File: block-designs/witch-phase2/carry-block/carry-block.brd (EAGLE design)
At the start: 27.9 x 27.9 mm, 13 parts, among them IC1 74AHC1G32DBV, IC2 74AHC1G86DBV, IC3 74LS195D, IC4 741G175

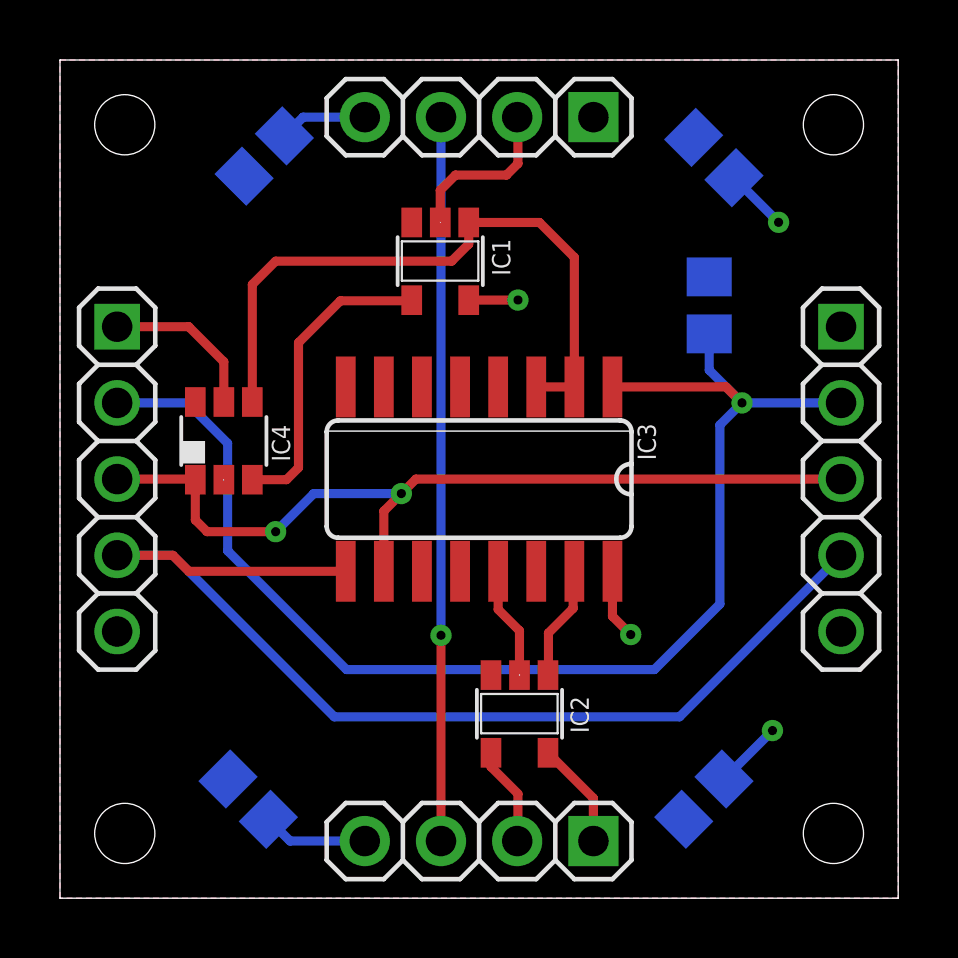
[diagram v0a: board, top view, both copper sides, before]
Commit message: adjust borders for ground/vcc plains and size to match 1.1inch grids
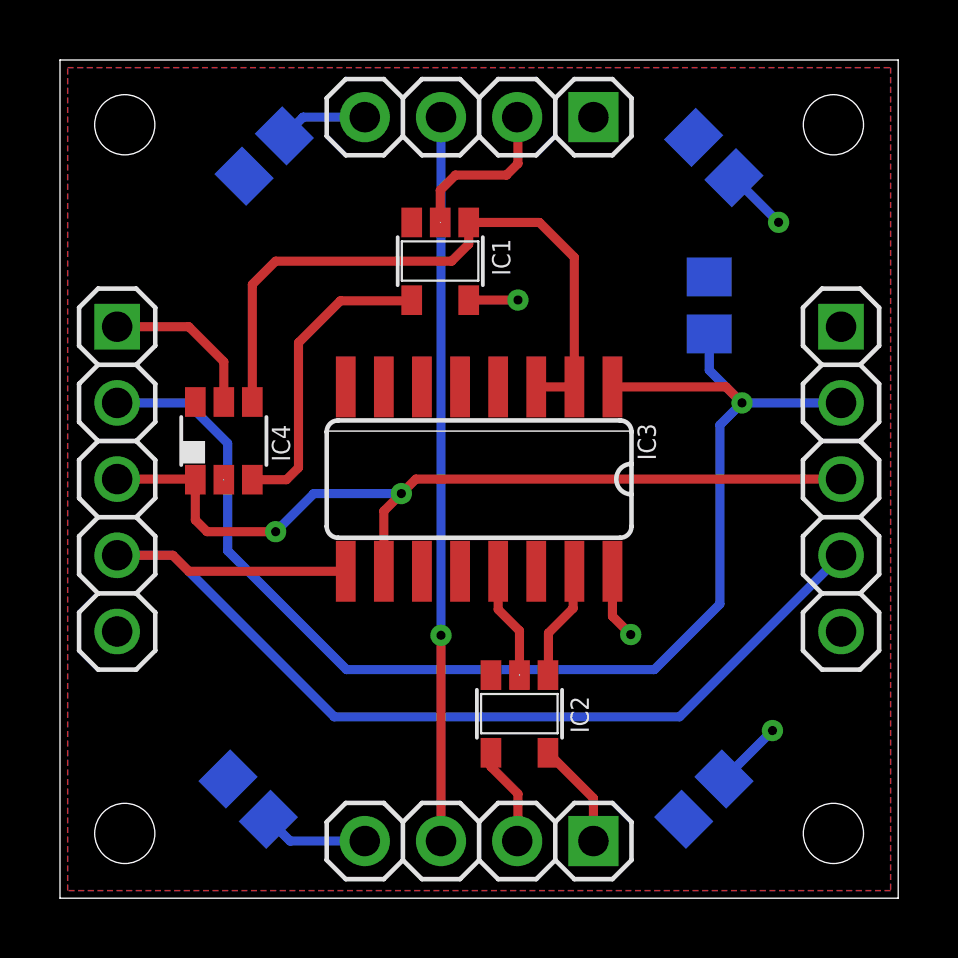
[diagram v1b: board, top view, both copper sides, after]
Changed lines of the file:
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@@
 <contactref element="JP1" pad="4"/>
 <contactref element="JP3" pad="4"/>
-<polygon width="0" layer="1">
-<vertex x="27.94" y="0"/>
-<vertex x="0" y="0"/>
-<vertex x="0" y="27.94"/>
-<vertex x="27.94" y="27.94"/>
+<polygon width="0.254" layer="1">
+<vertex x="27.686" y="0.254"/>
+<vertex x="0.254" y="0.254"/>
+<vertex x="0.254" y="27.686"/>
+<vertex x="27.686" y="27.686"/>
 </polygon>
 <contactref element="IC1" pad="3"/>
@@
 <contactref element="JP1" pad="1"/>
 <contactref element="JP3" pad="1"/>
-<polygon width="0" layer="16">
-<vertex x="27.94" y="0"/>
-<vertex x="0" y="0"/>
-<vertex x="0" y="27.94"/>
-<vertex x="27.94" y="27.94"/>
+<polygon width="0.254" layer="16">
+<vertex x="27.686" y="0.254"/>
+<vertex x="0.254" y="0.254"/>
+<vertex x="0.254" y="27.686"/>
+<vertex x="27.686" y="27.686"/>
 </polygon>
 <contactref element="JP4" pad="1"/>

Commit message: updated board layout pictures and pdf schematics
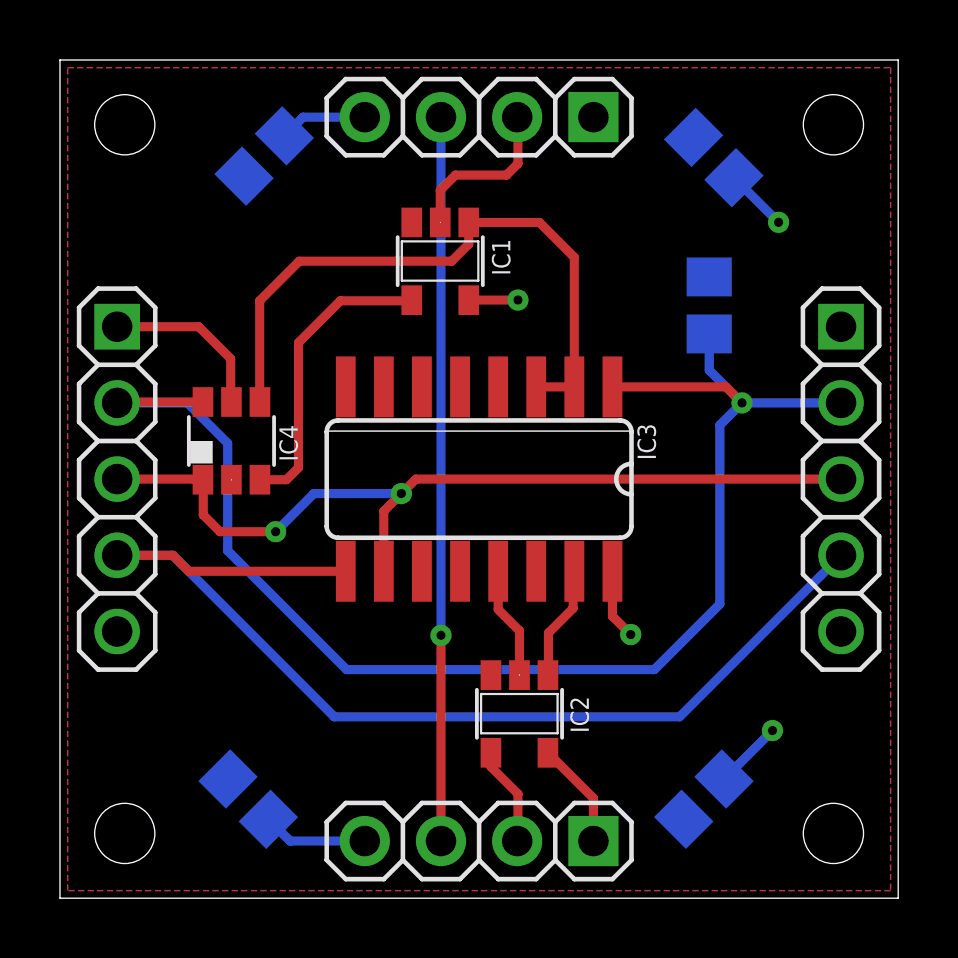
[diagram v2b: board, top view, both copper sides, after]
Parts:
- moved IC4 0.25 mm to (5.71, 15.2)
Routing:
- net !RST: track 44.4 -> 47.3 mm
- net ZC-OUT: track 22.1 -> 21.5 mm
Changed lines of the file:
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@@
 <text x="5.7912" y="25.4508" size="1.016" layer="48">TOP</text>
 <text x="19.3802" y="25.5016" size="1.016" layer="48">TOP</text>
-<text x="1.397" y="4.699" size="0.6096" layer="48">CARRY
-  UNIT</text>
+<text x="0.762" y="5.08" size="0.6096" layer="48">CARRY
+UNIT</text>
 </plain>
 <attributes>
@@
 <attribute name="VALUE" x="24.1808" y="20.3962" size="1.27" layer="28" rot="MR270"/>
 </element>
-<element name="IC4" library="74xx-little-us" package="DBV_R-PDSO-G6" value="741G175" x="5.461" y="15.24" smashed="yes">
-<attribute name="NAME" x="7.6708" y="14.5542" size="0.6096" layer="25" rot="R90"/>
-<attribute name="VALUE" x="3.556" y="12.065" size="1.27" layer="27"/>
+<element name="IC4" library="74xx-little-us" package="DBV_R-PDSO-G6" value="741G175" x="5.715" y="15.24" smashed="yes">
+<attribute name="NAME" x="7.9248" y="14.5542" size="0.6096" layer="25" rot="R90"/>
+<attribute name="VALUE" x="3.81" y="12.065" size="1.27" layer="27"/>
 </element>
 <element name="IC2" library="74xx-little-us" package="SOT23-5" value="74AHC1G86DBV" x="15.3162" y="6.1468" smashed="yes" rot="R180">
@@
 <wire x1="18.415" y1="9.398" x2="19.0246" y2="8.7884" width="0.3048" layer="1"/>
 <via x="19.0246" y="8.7884" extent="1-16" drill="0.3048"/>
-<wire x1="5.461" y1="16.54" x2="5.461" y2="17.8816" width="0.3048" layer="1"/>
-<wire x1="1.905" y1="19.05" x2="4.2926" y2="19.05" width="0.3048" layer="1"/>
-<wire x1="4.2926" y1="19.05" x2="5.461" y2="17.8816" width="0.3048" layer="1"/>
+<wire x1="1.905" y1="19.05" x2="4.6228" y2="19.05" width="0.3048" layer="1"/>
 <wire x1="16.2662" y1="4.8468" x2="17.78" y2="3.333" width="0.3048" layer="1"/>
 <wire x1="17.78" y1="3.333" x2="17.78" y2="1.905" width="0.3048" layer="1"/>
@@
 <wire x1="13.6292" y1="19.939" x2="15.2654" y2="19.939" width="0.3048" layer="1"/>
 <via x="15.2654" y="19.939" extent="1-16" drill="0.3048"/>
+<wire x1="4.6228" y1="19.05" x2="5.6896" y2="17.9832" width="0.3048" layer="1"/>
+<wire x1="5.6896" y1="17.9832" x2="5.6896" y2="16.5654" width="0.3048" layer="1"/>
+<wire x1="5.6896" y1="16.5654" x2="5.715" y2="16.54" width="0.3048" layer="1"/>
 </signal>
 <signal name="ZC">
@@
 <wire x1="15.875" y1="17.0434" x2="17.145" y2="17.0434" width="0.3048" layer="1"/>
 <wire x1="17.1196" y1="17.0688" x2="17.145" y2="17.0434" width="0.3048" layer="1"/>
-<wire x1="6.411" y1="16.54" x2="6.411" y2="20.4572" width="0.3048" layer="1"/>
 <wire x1="13.6398" y1="22.5396" x2="13.6246" y2="22.5244" width="0.3048" layer="1"/>
 <wire x1="13.6246" y1="22.5244" x2="15.982" y2="22.5244" width="0.3048" layer="1"/>
 <wire x1="15.982" y1="22.5244" x2="17.145" y2="21.3614" width="0.3048" layer="1"/>
 <wire x1="17.145" y1="21.3614" x2="17.145" y2="17.0434" width="0.3048" layer="1"/>
-<wire x1="6.411" y1="20.4572" x2="7.1882" y2="21.2344" width="0.3048" layer="1"/>
-<wire x1="7.1882" y1="21.2344" x2="13.0556" y2="21.2344" width="0.3048" layer="1"/>
 <wire x1="13.0556" y1="21.2344" x2="13.6246" y2="21.8034" width="0.3048" layer="1"/>
 <wire x1="13.6246" y1="21.8034" x2="13.6246" y2="22.5244" width="0.3048" layer="1"/>
+<wire x1="13.0556" y1="21.2344" x2="7.9756" y2="21.2344" width="0.3048" layer="1"/>
+<wire x1="7.9756" y1="21.2344" x2="6.6548" y2="19.9136" width="0.3048" layer="1"/>
+<wire x1="6.6548" y1="19.9136" x2="6.6548" y2="16.5502" width="0.3048" layer="1"/>
+<wire x1="6.6548" y1="16.5502" x2="6.665" y2="16.54" width="0.3048" layer="1"/>
 </signal>
 <signal name="N$5">
 <contactref element="IC1" pad="4"/>
 <contactref element="IC4" pad="3"/>
-<wire x1="6.411" y1="13.95" x2="7.5492" y2="13.95" width="0.3048" layer="1"/>
 <wire x1="7.9502" y1="14.351" x2="7.5492" y2="13.95" width="0.3048" layer="1"/>
 <wire x1="7.9502" y1="14.351" x2="7.9502" y2="18.5166" width="0.3048" layer="1"/>
@@
 <wire x1="9.3472" y1="19.9136" x2="11.7038" y2="19.9136" width="0.3048" layer="1"/>
 <wire x1="11.7038" y1="19.9136" x2="11.7246" y2="19.9344" width="0.3048" layer="1"/>
+<wire x1="7.5492" y1="13.95" x2="6.665" y2="13.95" width="0.3048" layer="1"/>
 </signal>
 <signal name="!MCLK">
@@
 <contactref element="IC4" pad="1"/>
 <wire x1="1.905" y1="13.97" x2="4.491" y2="13.97" width="0.3048" layer="1"/>
-<wire x1="4.491" y1="13.97" x2="4.511" y2="13.95" width="0.3048" layer="1"/>
-<wire x1="4.4958" y1="13.9348" x2="4.511" y2="13.95" width="0.3048" layer="1"/>
+<wire x1="4.491" y1="13.97" x2="4.765" y2="13.95" width="0.3048" layer="1"/>
+<wire x1="4.4958" y1="13.9348" x2="4.765" y2="13.95" width="0.3048" layer="1"/>
 <contactref element="IC3" pad="10"/>
 <wire x1="26.035" y1="13.97" x2="11.8618" y2="13.97" width="0.3048" layer="1"/>
@@
 <wire x1="10.795" y1="12.9032" x2="10.795" y2="10.8966" width="0.3048" layer="1"/>
 <via x="11.3792" y="13.4874" extent="1-16" drill="0.3048"/>
-<wire x1="4.511" y1="13.95" x2="4.511" y2="12.6086" width="0.3048" layer="1"/>
-<wire x1="4.511" y1="12.6086" x2="4.9022" y2="12.2174" width="0.3048" layer="1"/>
-<wire x1="4.9022" y1="12.2174" x2="7.1882" y2="12.2174" width="0.3048" layer="1"/>
 <via x="7.1882" y="12.2174" extent="1-16" drill="0.3048"/>
 <wire x1="7.1882" y1="12.2174" x2="8.4582" y2="13.4874" width="0.3048" layer="16"/>
 <wire x1="8.4582" y1="13.4874" x2="11.3792" y2="13.4874" width="0.3048" layer="16"/>
+<wire x1="7.1882" y1="12.2174" x2="5.334" y2="12.2174" width="0.3048" layer="1"/>
+<wire x1="5.334" y1="12.2174" x2="4.7752" y2="12.7762" width="0.3048" layer="1"/>
+<wire x1="4.7752" y1="12.7762" x2="4.7752" y2="13.9398" width="0.3048" layer="1"/>
+<wire x1="4.7752" y1="13.9398" x2="4.765" y2="13.95" width="0.3048" layer="1"/>
 </signal>
 <signal name="!RST">
@@
 <wire x1="22.1996" y1="17.0434" x2="22.733" y2="16.51" width="0.3048" layer="1"/>
 <wire x1="21.6408" y1="17.6022" x2="21.6408" y2="18.8112" width="0.3048" layer="16"/>
-<wire x1="4.2418" y1="16.51" x2="4.511" y2="16.54" width="0" layer="19" extent="1-16"/>
+<wire x1="4.765" y1="16.54" x2="1.935" y2="16.54" width="0.3048" layer="1"/>
+<wire x1="1.935" y1="16.54" x2="1.905" y2="16.51" width="0.3048" layer="1"/>
 </signal>
 <signal name="CARRY_EN">

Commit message: updated designs for new labeling and spacing
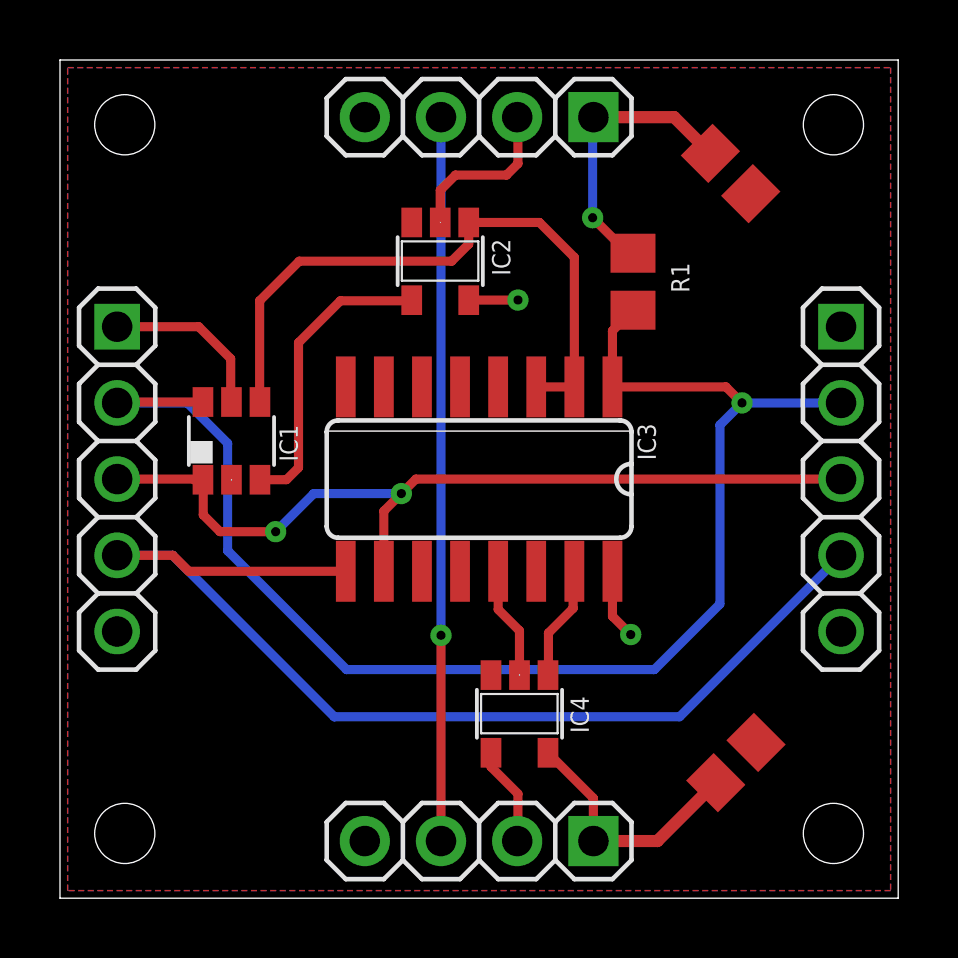
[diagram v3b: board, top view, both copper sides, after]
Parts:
- removed C3, C4: (no value), resistor:C0805
- IC1: value 74AHC1G32DBV -> 741G175; device 74xx-little-us:SOT23-5 -> 74xx-little-us:DBV_R-PDSO-G6
- IC2: value 74AHC1G86DBV -> 74AHC1G32DBV
- IC4: value 741G175 -> 74AHC1G86DBV; device 74xx-little-us:DBV_R-PDSO-G6 -> 74xx-little-us:SOT23-5
- moved C2 15.6 mm to (22.4, 24.2), flipped to the top, turned to 315 degrees
- moved IC2 15.3 mm to (12.7, 21.2)
- moved IC4 13.2 mm to (15.3, 6.15), turned to 180 degrees
- moved IC1 9.19 mm to (5.71, 15.2), turned to 0 degrees
- moved R1 2.66 mm to (19.1, 20.5), flipped to the top
- moved C1 1.62 mm to (22.5, 4.52), flipped to the top, turned to 45 degrees
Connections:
- net !MCLK: now also IC1.1; no longer IC4.1
- net !RST: now also IC1.6; no longer IC4.6
- net CARRY_EN: now also IC4.4; no longer IC2.4
- net GND: now also IC1.2, IC4.3; no longer C3.2, C4.2, IC1.3, IC4.2
- net N$1: now also IC4.1; no longer IC2.1
- net N$2: now also IC4.2; no longer IC2.2
- net N$5: now also IC1.3, IC2.4; no longer IC1.4, IC4.3
- net VCC: no longer C3.1, C4.1
- net ZC: now also IC2.2; no longer IC1.2
- net ZC-OUT: now also IC1.4, IC2.1; no longer IC1.1, IC4.4
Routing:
- net VCC: track 13.3 -> 27.7 mm, vias 2 -> 3
- net GND: track 10.8 -> 0.00 mm, vias 2 -> 0
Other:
- board text removed: "TOP"
